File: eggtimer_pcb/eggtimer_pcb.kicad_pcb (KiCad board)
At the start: 2 copper layers, 71.1 x 71.1 mm, 84 parts, among them J1 Conn_01x03, Q1 CPH3350-TL-W, Q10 2N7002P,215, Q2 CPH3350-TL-W, Q3 CPH3350-TL-W, Q4 CPH3350-TL-W, Q5 CPH3350-TL-W, Q6 CPH3350-TL-W, Q7 CPH3350-TL-W, Q8 CPH3350-TL-W, Q9 2N7002P,215, SW1 Rotary_Encoder_Switch, SW2 SW_Push, U1 BD70522GUL-E2, U2 STM32G051GxU, Y1 32.xxxk

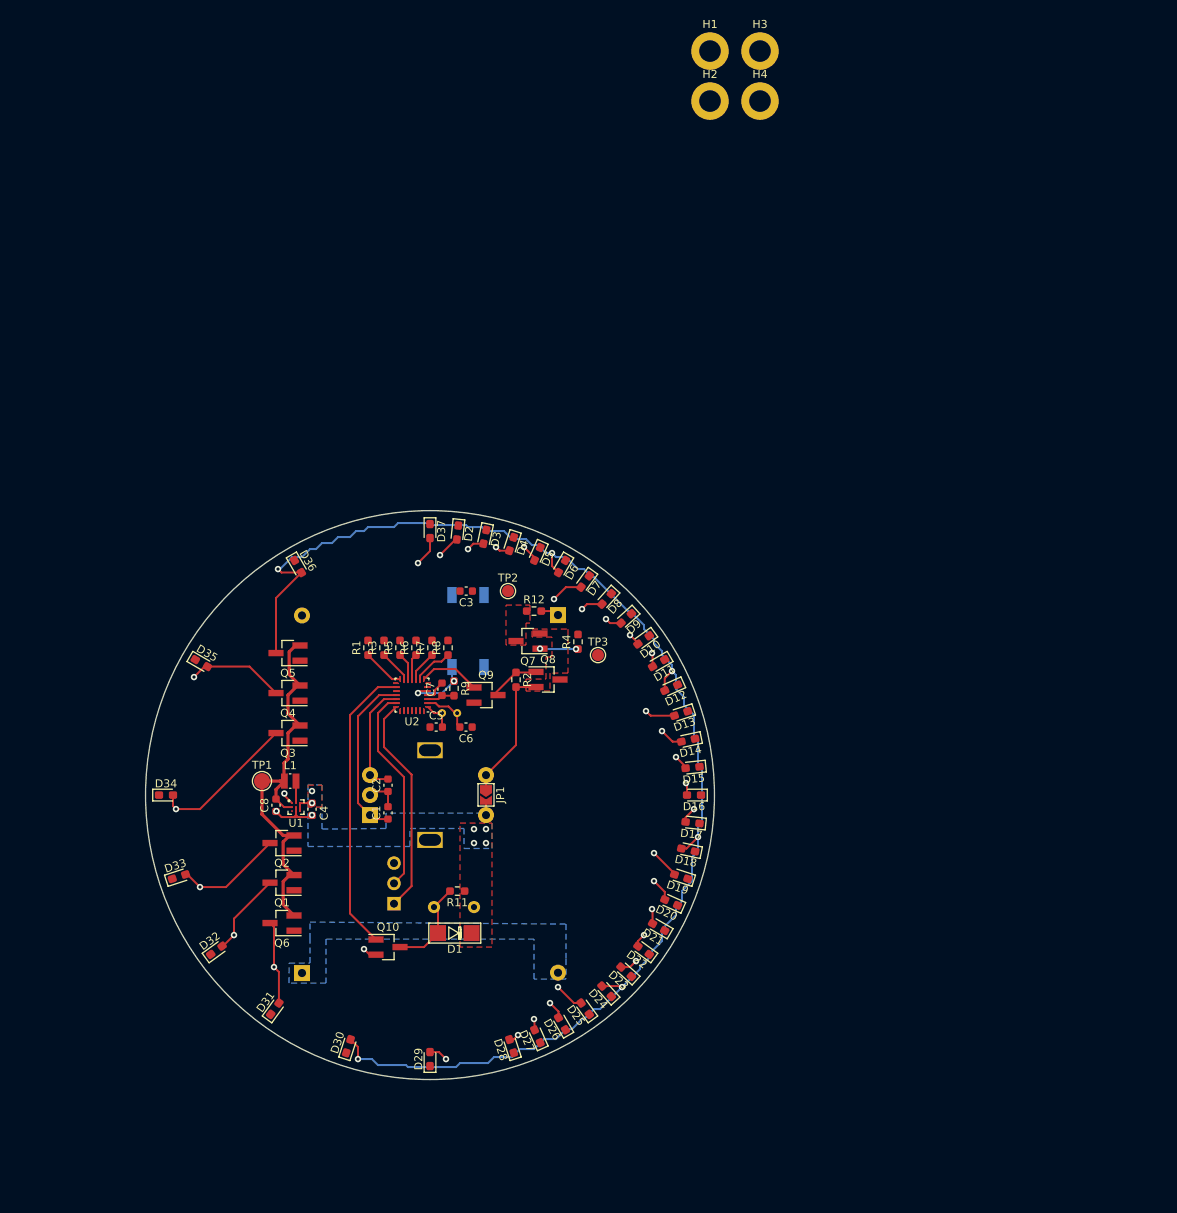
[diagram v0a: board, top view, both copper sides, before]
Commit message: Add pcb rev2
also design planetary gears for mechanics and make sure they fit
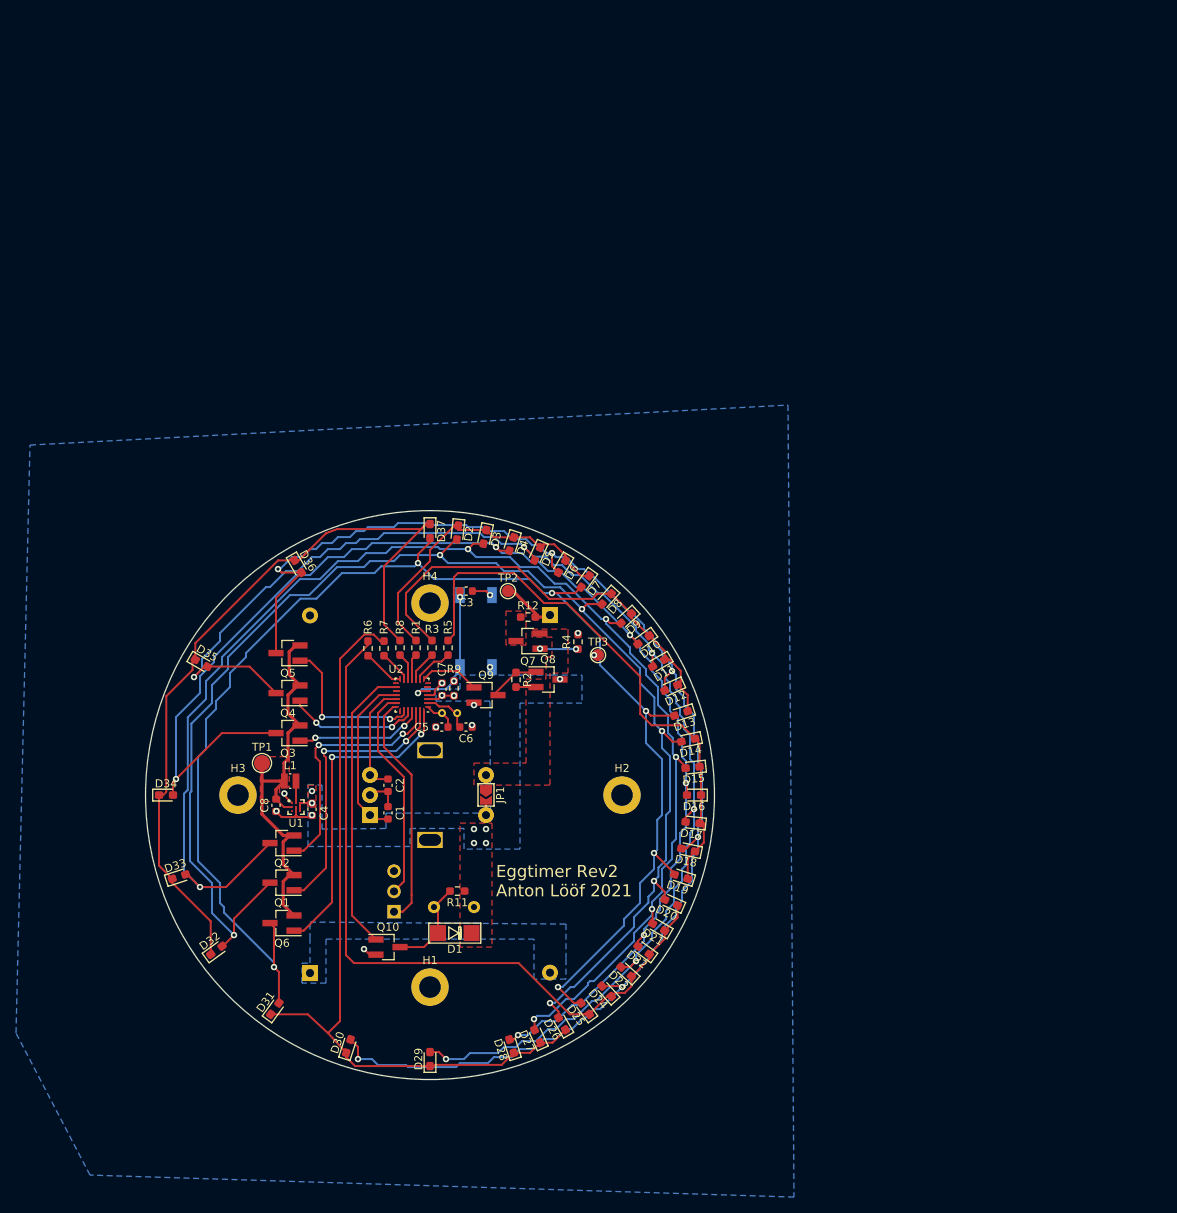
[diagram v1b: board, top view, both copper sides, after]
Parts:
- moved H1 122.1 mm to (141.0, 140.0)
- moved H3 113.6 mm to (117.0, 116.0)
- moved H2 87.4 mm to (165.0, 116.0)
- moved H4 75.1 mm to (141.0, 92.0)
- moved R6 6.00 mm to (133.2, 97.7)
- moved R7 6.00 mm to (135.2, 97.7)
- moved R1 6.00 mm to (139.2, 97.6)
- moved R3 6.00 mm to (141.2, 97.6)
- moved R5 6.00 mm to (143.2, 97.6)
- moved R8 6.00 mm to (137.2, 97.6)
- moved TP1 2.25 mm to (120.0, 112.0)
- moved R12 1.06 mm to (153.2, 93.8)
- moved BT1 1.00 mm to (156.0, 93.5)
- moved BT2 1.00 mm to (126.0, 138.2)
- moved J1 1.00 mm to (136.5, 130.6)
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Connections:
- R1 pad 1: led_c0 -> led_c3
- R3 pad 1: led_c1 -> led_c4
- R5 pad 1: led_c2 -> led_c5
- R6 pad 1: led_c3 -> led_c0
- R7 pad 1: led_c4 -> led_c1
- R8 pad 1: led_c5 -> led_c2
- U1 pad C1: Net-(U1-PadC1) -> (no net)
- U2 pad 15: Net-(U2-Pad15) -> (no net)
- U2 pad 17: Net-(U2-Pad17) -> (no net)
- U2 pad 22: Net-(U2-Pad22) -> (no net)
- U2 pad 23: led_a0 -> led_a4
- U2 pad 24: led_a1 -> led_a3
- U2 pad 26: led_a3 -> led_a1
- U2 pad 27: led_a4 -> led_a0
- U2 pad 6: Net-(U2-Pad6) -> (no net)
- U2 pad 7: Net-(U2-Pad7) -> (no net)
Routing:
- net Net-(D14-Pad2): track 24.3 -> 176.2 mm
- net Net-(D15-Pad2): track 22.9 -> 174.6 mm
- net Net-(D13-Pad2): track 29.4 -> 180.5 mm
- net Net-(D11-Pad2): track 22.7 -> 168.1 mm
- net Net-(D10-Pad2): track 26.3 -> 168.8 mm
- net Net-(D32-Pad1): track 0.00 -> 96.7 mm
- net Net-(D26-Pad1): track 0.00 -> 96.2 mm
- net Net-(D20-Pad1): track 0.00 -> 93.1 mm
- net Net-(D14-Pad1): track 0.00 -> 69.5 mm
- net Net-(D10-Pad1): track 0.00 -> 55.5 mm
- net led_a5: track 0.00 -> 39.7 mm, vias 0 -> 2
- net Net-(D2-Pad1): track 0.00 -> 38.7 mm
- net led_a0: track 0.00 -> 35.2 mm, vias 0 -> 2
- net led_a1: track 0.00 -> 30.7 mm, vias 0 -> 2
- net led_a4: track 0.00 -> 20.0 mm, vias 0 -> 2
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- added copper zone on F.Cu, net 2v_led
- added copper zone on B.Cu, net GND
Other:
- board text added: "Eggtimer Rev2 Anton Lööf 2021"

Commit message: MORE LEDS
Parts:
- added D38: TLMS1000-GS08, LED_SMD:LED_0603_1608Metric_Pad1.05x0.95mm_HandSolder, F.Cu at (118.9, 140.5)
- added D39: TLMS1000-GS08, LED_SMD:LED_0603_1608Metric_Pad1.05x0.95mm_HandSolder, F.Cu at (116.5, 138.1)
- added D40: TLMS1000-GS08, LED_SMD:LED_0603_1608Metric_Pad1.05x0.95mm_HandSolder, F.Cu at (114.3, 135.4)
- added D41: TLMS1000-GS08, LED_SMD:LED_0603_1608Metric_Pad1.05x0.95mm_HandSolder, F.Cu at (112.4, 132.5)
- added D42: TLMS1000-GS08, LED_SMD:LED_0603_1608Metric_Pad1.05x0.95mm_HandSolder, F.Cu at (110.9, 129.4)
- added D43: TLMS1000-GS08, LED_SMD:LED_0603_1608Metric_Pad1.05x0.95mm_HandSolder, F.Cu at (109.6, 126.2)
- added D44: TLMS1000-GS08, LED_SMD:LED_0603_1608Metric_Pad1.05x0.95mm_HandSolder, F.Cu at (108.7, 122.9)
- added D45: TLMS1000-GS08, LED_SMD:LED_0603_1608Metric_Pad1.05x0.95mm_HandSolder, F.Cu at (108.2, 119.4)
- added D46: TLMS1000-GS08, LED_SMD:LED_0603_1608Metric_Pad1.05x0.95mm_HandSolder, F.Cu at (108.0, 116.0)
- added D47: TLMS1000-GS08, LED_SMD:LED_0603_1608Metric_Pad1.05x0.95mm_HandSolder, F.Cu at (108.2, 112.6)
- added D48: TLMS1000-GS08, LED_SMD:LED_0603_1608Metric_Pad1.05x0.95mm_HandSolder, F.Cu at (108.7, 109.1)
- added D49: TLMS1000-GS08, LED_SMD:LED_0603_1608Metric_Pad1.05x0.95mm_HandSolder, F.Cu at (109.6, 105.8)
- added D50: TLMS1000-GS08, LED_SMD:LED_0603_1608Metric_Pad1.05x0.95mm_HandSolder, F.Cu at (110.9, 102.6)
- added D51: TLMS1000-GS08, LED_SMD:LED_0603_1608Metric_Pad1.05x0.95mm_HandSolder, F.Cu at (112.4, 99.5)
- added D52: TLMS1000-GS08, LED_SMD:LED_0603_1608Metric_Pad1.05x0.95mm_HandSolder, F.Cu at (114.3, 96.6)
- added D53: TLMS1000-GS08, LED_SMD:LED_0603_1608Metric_Pad1.05x0.95mm_HandSolder, F.Cu at (116.5, 93.9)
- added D54: TLMS1000-GS08, LED_SMD:LED_0603_1608Metric_Pad1.05x0.95mm_HandSolder, F.Cu at (118.9, 91.5)
- added D55: TLMS1000-GS08, LED_SMD:LED_0603_1608Metric_Pad1.05x0.95mm_HandSolder, F.Cu at (121.6, 89.3)
- added D56: TLMS1000-GS08, LED_SMD:LED_0603_1608Metric_Pad1.05x0.95mm_HandSolder, F.Cu at (124.5, 87.4)
- added D57: TLMS1000-GS08, LED_SMD:LED_0603_1608Metric_Pad1.05x0.95mm_HandSolder, F.Cu at (127.6, 85.9)
- added D58: TLMS1000-GS08, LED_SMD:LED_0603_1608Metric_Pad1.05x0.95mm_HandSolder, F.Cu at (130.8, 84.6)
- added D59: TLMS1000-GS08, LED_SMD:LED_0603_1608Metric_Pad1.05x0.95mm_HandSolder, F.Cu at (134.1, 83.7)
- added D60: TLMS1000-GS08, LED_SMD:LED_0603_1608Metric_Pad1.05x0.95mm_HandSolder, F.Cu at (137.6, 83.2)
- added D61: TLMS1000-GS08, LED_SMD:LED_0603_1608Metric_Pad1.05x0.95mm_HandSolder, F.Cu at (141.0, 83.0)
- added Q11: CPH3350-TL-W, Package_TO_SOT_SMD:SOT-23_Handsoldering, F.Cu at (194.9, 79.4)
- added Q12: CPH3350-TL-W, Package_TO_SOT_SMD:SOT-23_Handsoldering, F.Cu at (201.3, 88.5)
- added R10: 200, Resistor_SMD:R_0603_1608Metric_Pad0.98x0.95mm_HandSolder, F.Cu at (224.6, 99.0)
- added R13: 200, Resistor_SMD:R_0603_1608Metric_Pad0.98x0.95mm_HandSolder, F.Cu at (224.5, 101.5)
- moved R8 94.0 mm to (231.0, 91.3), turned to 0 degrees
- moved R6 93.4 mm to (226.6, 93.9), turned to 0 degrees
- moved Q2 89.6 mm to (201.3, 79.4), turned to 0 degrees
- moved R7 89.3 mm to (224.6, 96.5), turned to 0 degrees
- moved Q5 86.6 mm to (207.8, 79.4), turned to 0 degrees
- moved Q1 84.2 mm to (194.9, 83.9), turned to 0 degrees
- moved Q6 82.2 mm to (194.9, 93.0), turned to 0 degrees
- moved R1 80.9 mm to (220.2, 99.1), turned to 0 degrees
- moved Q4 80.4 mm to (201.3, 83.9), turned to 0 degrees
- moved R3 79.0 mm to (220.2, 101.6), turned to 0 degrees
- moved Q3 74.3 mm to (194.9, 88.5), turned to 0 degrees
- moved D37 62.8 mm to (121.6, 142.7), turned to 54 degrees
- moved D36 57.2 mm to (124.5, 144.6), turned to 60 degrees
- moved D35 49.0 mm to (127.6, 146.1), turned to 66 degrees
- moved D34 38.8 mm to (130.8, 147.4), turned to 72 degrees
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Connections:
- net /power_on renamed Net-(Q8-Pad1)
- D14 pad 1: Net-(D14-Pad1) -> Net-(D10-Pad1)
- D15 pad 1: Net-(D14-Pad1) -> Net-(D10-Pad1)
- D16 pad 1: Net-(D14-Pad1) -> Net-(D10-Pad1)
- D16 pad 2: Net-(D10-Pad2) -> Net-(D16-Pad2)
- D17 pad 1: Net-(D14-Pad1) -> Net-(D10-Pad1)
- D17 pad 2: Net-(D11-Pad2) -> Net-(D17-Pad2)
- D18 pad 1: Net-(D14-Pad1) -> Net-(D18-Pad1)
- D18 pad 2: Net-(D12-Pad2) -> Net-(D10-Pad2)
- D19 pad 1: Net-(D14-Pad1) -> Net-(D18-Pad1)
- D19 pad 2: Net-(D13-Pad2) -> Net-(D11-Pad2)
- D2 pad 2: Net-(D14-Pad2) -> Net-(D10-Pad2)
- D20 pad 1: Net-(D20-Pad1) -> Net-(D18-Pad1)
- D20 pad 2: Net-(D14-Pad2) -> Net-(D12-Pad2)
- D21 pad 1: Net-(D20-Pad1) -> Net-(D18-Pad1)
- D21 pad 2: Net-(D15-Pad2) -> Net-(D13-Pad2)
- D22 pad 1: Net-(D20-Pad1) -> Net-(D18-Pad1)
- D22 pad 2: Net-(D10-Pad2) -> Net-(D14-Pad2)
- D23 pad 1: Net-(D20-Pad1) -> Net-(D18-Pad1)
- D23 pad 2: Net-(D11-Pad2) -> Net-(D15-Pad2)
- D24 pad 1: Net-(D20-Pad1) -> Net-(D18-Pad1)
- D24 pad 2: Net-(D12-Pad2) -> Net-(D16-Pad2)
- D25 pad 1: Net-(D20-Pad1) -> Net-(D18-Pad1)
- D25 pad 2: Net-(D13-Pad2) -> Net-(D17-Pad2)
- D26 pad 2: Net-(D14-Pad2) -> Net-(D10-Pad2)
- D27 pad 2: Net-(D15-Pad2) -> Net-(D11-Pad2)
- D28 pad 2: Net-(D10-Pad2) -> Net-(D12-Pad2)
- D29 pad 2: Net-(D11-Pad2) -> Net-(D13-Pad2)
- D3 pad 2: Net-(D15-Pad2) -> Net-(D11-Pad2)
- D30 pad 2: Net-(D12-Pad2) -> Net-(D14-Pad2)
- D31 pad 2: Net-(D13-Pad2) -> Net-(D15-Pad2)
- D32 pad 1: Net-(D32-Pad1) -> Net-(D26-Pad1)
- D32 pad 2: Net-(D14-Pad2) -> Net-(D16-Pad2)
- D33 pad 1: Net-(D32-Pad1) -> Net-(D26-Pad1)
- D33 pad 2: Net-(D15-Pad2) -> Net-(D17-Pad2)
- D34 pad 1: Net-(D32-Pad1) -> Net-(D34-Pad1)
- D35 pad 1: Net-(D32-Pad1) -> Net-(D34-Pad1)
- D36 pad 1: Net-(D32-Pad1) -> Net-(D34-Pad1)
- D37 pad 1: Net-(D32-Pad1) -> Net-(D34-Pad1)
- D4 pad 2: Net-(D10-Pad2) -> Net-(D12-Pad2)
- D5 pad 2: Net-(D11-Pad2) -> Net-(D13-Pad2)
- D6 pad 2: Net-(D12-Pad2) -> Net-(D14-Pad2)
- D7 pad 2: Net-(D13-Pad2) -> Net-(D15-Pad2)
- D8 pad 1: Net-(D10-Pad1) -> Net-(D2-Pad1)
- D8 pad 2: Net-(D14-Pad2) -> Net-(D16-Pad2)
- D9 pad 1: Net-(D10-Pad1) -> Net-(D2-Pad1)
- D9 pad 2: Net-(D15-Pad2) -> Net-(D17-Pad2)
- Q1 pad 1: led_a0 -> led_a7
- Q1 pad 3: Net-(D14-Pad2) -> Net-(D10-Pad2)
- Q2 pad 1: led_a1 -> led_a6
- Q2 pad 3: Net-(D15-Pad2) -> Net-(D11-Pad2)
- Q3 pad 1: led_a2 -> led_a5
- Q3 pad 3: Net-(D10-Pad2) -> Net-(D12-Pad2)
- Q4 pad 1: led_a3 -> led_a4
- Q4 pad 3: Net-(D11-Pad2) -> Net-(D13-Pad2)
- Q5 pad 1: led_a4 -> led_a3
- Q5 pad 3: Net-(D12-Pad2) -> Net-(D14-Pad2)
- Q6 pad 1: led_a5 -> led_a2
- Q6 pad 3: Net-(D13-Pad2) -> Net-(D15-Pad2)
- R1 pad 1: led_c3 -> led_c7
- R3 pad 1: led_c4 -> led_c6
- R5 pad 2: Net-(D14-Pad1) -> Net-(D18-Pad1)
- R6 pad 1: led_c0 -> led_c4
- R6 pad 2: Net-(D20-Pad1) -> Net-(D26-Pad1)
- R7 pad 1: led_c1 -> led_c3
- R7 pad 2: Net-(D26-Pad1) -> Net-(D34-Pad1)
- R8 pad 2: Net-(D32-Pad1) -> Net-(D42-Pad1)
- U1 pad C1: (no net) -> Net-(U1-PadC1)
- U2 pad 15: (no net) -> led_c7
- U2 pad 17: (no net) -> led_a7
- U2 pad 22: (no net) -> led_a6
- U2 pad 6: (no net) -> Net-(U2-Pad6)
- U2 pad 7: (no net) -> power_ctrl
- U2 pad 8: power_ctrl -> led_c6
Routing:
- net Net-(D13-Pad2): track 180.5 -> 0.00 mm, vias 6 -> 0
- net Net-(D14-Pad2): track 176.2 -> 0.00 mm, vias 6 -> 0
- net Net-(D15-Pad2): track 174.6 -> 0.00 mm, vias 6 -> 0
- net Net-(D12-Pad2): track 171.5 -> 0.00 mm, vias 6 -> 0
- net Net-(D10-Pad2): track 168.8 -> 0.00 mm, vias 6 -> 0
- net Net-(D11-Pad2): track 168.1 -> 0.00 mm, vias 6 -> 0
- net Net-(D32-Pad1): track 96.7 -> 0.00 mm
- net Net-(D26-Pad1): track 96.2 -> 0.00 mm
- net Net-(D20-Pad1): track 93.1 -> 0.00 mm
- net Net-(D14-Pad1): track 69.5 -> 0.00 mm
- net Net-(D10-Pad1): track 55.5 -> 0.00 mm
- net 2v_led: track 53.3 -> 2.41 mm
- net led_a5: track 39.7 -> 0.00 mm, vias 2 -> 0
- net Net-(D2-Pad1): track 38.7 -> 0.00 mm
- net led_a0: track 35.2 -> 0.00 mm, vias 2 -> 0
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
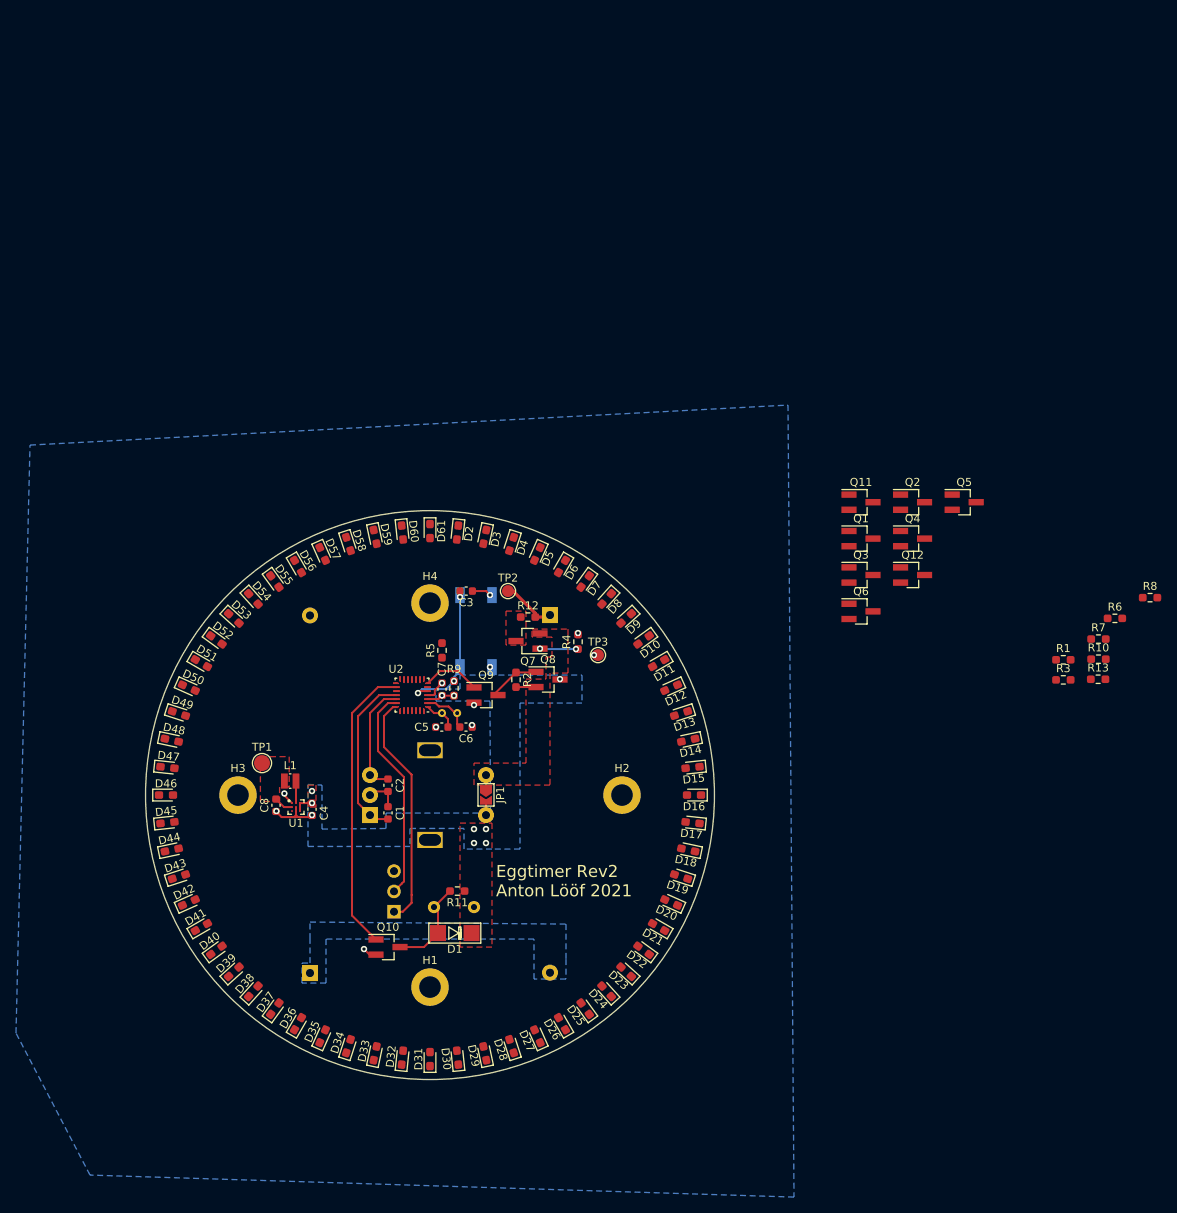
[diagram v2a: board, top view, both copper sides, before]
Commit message: Finalize rev2.1 pcb
make sure that schema is up to date with stmcubemx
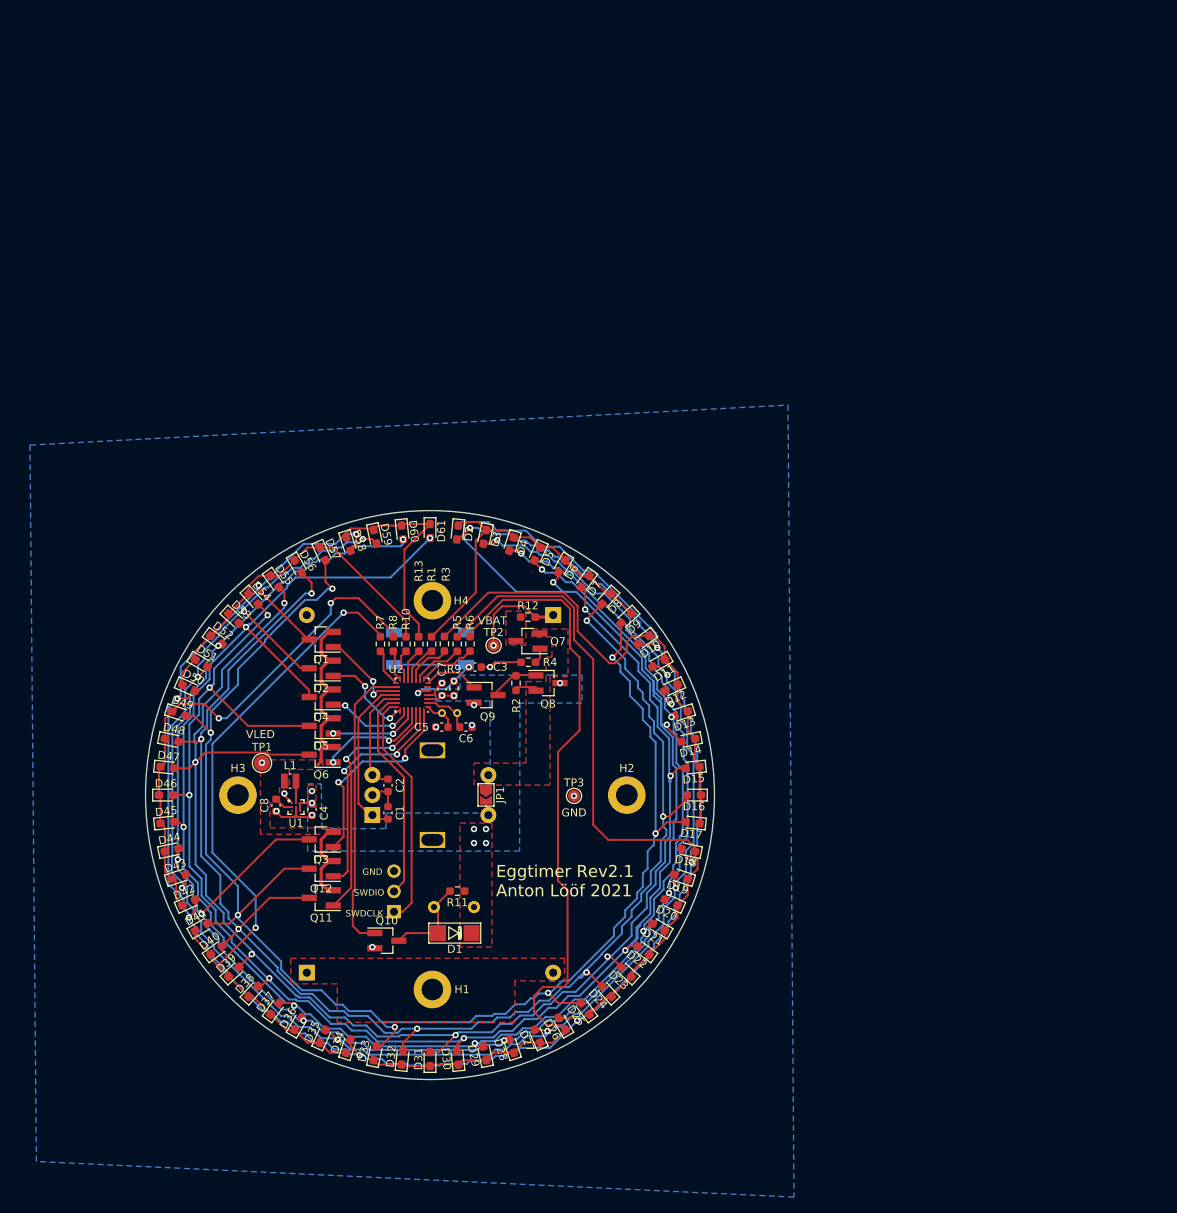
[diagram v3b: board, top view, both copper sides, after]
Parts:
- moved R8 94.8 mm to (136.4, 97.1), turned to 90 degrees
- moved R7 89.8 mm to (134.8, 97.1), turned to 90 degrees
- moved R10 86.6 mm to (138.0, 97.1), turned to 90 degrees
- moved Q5 85.1 mm to (127.4, 107.3), turned to 180 degrees
- moved R13 85.0 mm to (139.6, 97.1), turned to 90 degrees
- moved Q11 83.7 mm to (127.4, 128.8), turned to 180 degrees
- moved Q12 82.5 mm to (127.4, 125.2), turned to 180 degrees
- moved R6 80.7 mm to (146.0, 97.1), turned to 90 degrees
- moved R1 79.0 mm to (141.2, 97.1), turned to 90 degrees
- moved R3 77.5 mm to (142.8, 97.1), turned to 90 degrees
- moved Q2 76.8 mm to (127.4, 100.2), turned to 180 degrees
- moved Q4 76.5 mm to (127.4, 103.8), turned to 180 degrees
- moved Q3 75.1 mm to (127.4, 121.5), turned to 180 degrees
- moved Q6 69.8 mm to (127.4, 111.0), turned to 180 degrees
- moved Q1 68.6 mm to (127.4, 96.5), turned to 180 degrees
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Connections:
- U2 pad 10: led_c4 -> led_c6
- U2 pad 11: led_c3 -> led_c7
- U2 pad 12: led_c2 -> led_c0
- U2 pad 14: led_c0 -> led_c2
- U2 pad 15: led_c7 -> led_c3
- U2 pad 8: led_c6 -> led_c4
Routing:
- net Net-(D14-Pad2): track 0.00 -> 251.8 mm, vias 0 -> 8
- net Net-(D10-Pad2): track 0.00 -> 237.1 mm, vias 0 -> 9
- net Net-(D11-Pad2): track 0.00 -> 228.4 mm, vias 0 -> 9
- net Net-(D12-Pad2): track 0.00 -> 223.4 mm, vias 0 -> 9
- net Net-(D13-Pad2): track 0.00 -> 216.4 mm, vias 0 -> 8
- net Net-(D15-Pad2): track 0.00 -> 191.0 mm, vias 0 -> 7
- net Net-(D17-Pad2): track 0.00 -> 189.9 mm, vias 0 -> 7
- net Net-(D16-Pad2): track 0.00 -> 188.4 mm, vias 0 -> 7
- net Net-(D26-Pad1): track 0.00 -> 101.9 mm
- net Net-(D34-Pad1): track 0.00 -> 87.2 mm, vias 0 -> 2
- net Net-(D18-Pad1): track 0.00 -> 86.2 mm
- net Net-(D42-Pad1): track 0.00 -> 64.2 mm, vias 0 -> 2
- net Net-(D10-Pad1): track 0.00 -> 62.1 mm
- net Net-(D50-Pad1): track 0.00 -> 43.2 mm
- net Net-(D2-Pad1): track 0.00 -> 42.7 mm
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- added copper zone on F.Cu, net /bat_center
- removed copper zone on B.Cu, net /bat_center
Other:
- board text added: "Eggtimer Rev2.1 Anton Lööf 2021"
- board text added: "GND"
- board text added: "SWDCLK"
- board text added: "SWDIO"
- board text added: "VBAT"
- board text added: "VLED"
- board text removed: "Eggtimer Rev2 Anton Lööf 2021"
